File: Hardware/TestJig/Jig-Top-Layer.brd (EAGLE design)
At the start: 62.2 x 54.6 mm, 7 parts

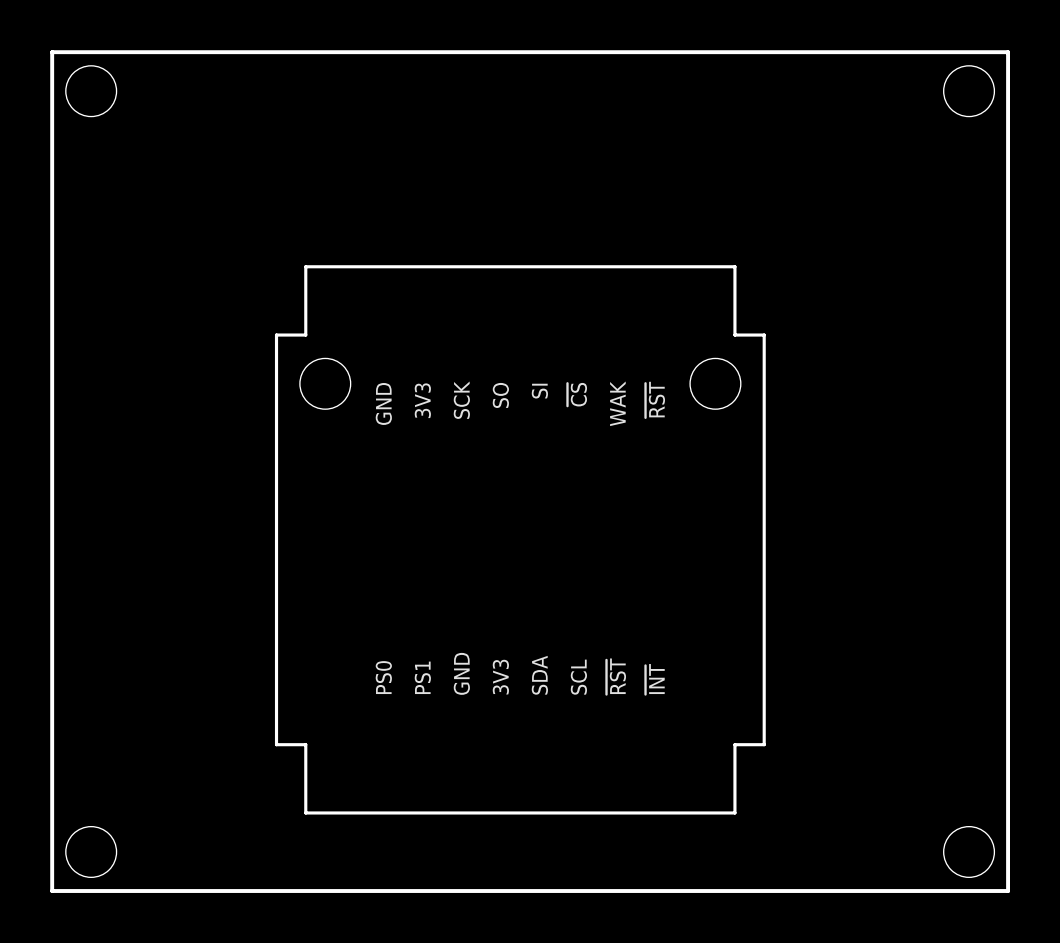
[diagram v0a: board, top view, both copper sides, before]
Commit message: Tweaked testjig middle and top layers
middle layer changes:
-changed holes for the pogopins to pup up through from pads to actual "holes" in eagle file. removed pads from sch and board.
-set hole size to 0.055 inch diameter for optimal lazer cutting in acrylic.

top layer changes:
-tightened up frame to huge product dimensions with 0.016 inch gap.
-added corner cutouts
-added "lift-out" cutout on the side, for easier product removal

Also note, bumped outer dimensions on both middle and top to allow for more strength around the corner standoff holes. Previous deisgn would probably crack if cut in acrylic with lazer.
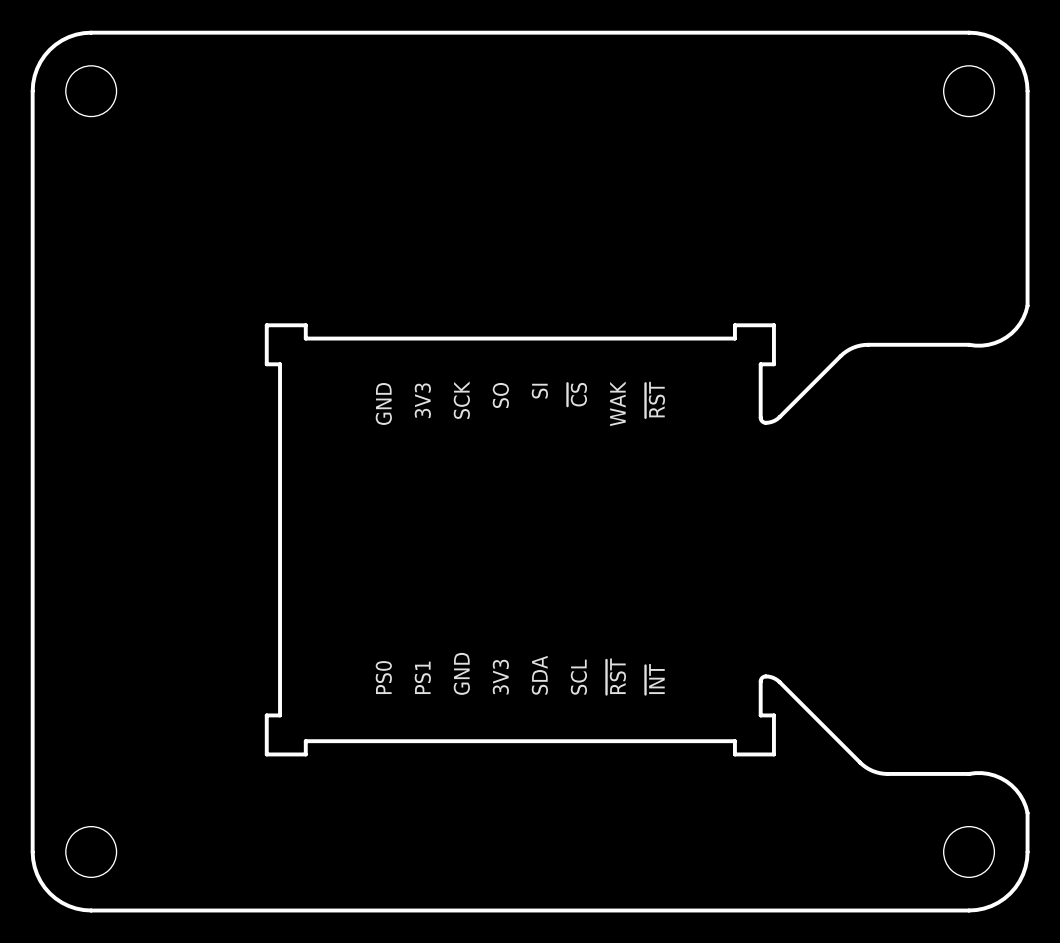
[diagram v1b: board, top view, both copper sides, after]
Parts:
- removed JP3, JP4: STAND-OFF, SparkFun:STAND-OFF
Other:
- board size 62.2 x 54.6 mm -> 64.8 x 57.2 mm
